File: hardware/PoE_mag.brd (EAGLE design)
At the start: 149.9 x 124.5 mm, 128 parts, among them IC1 LD1117V33, IC10 74LVC1T45SOT23-HAND, IC11 74LVC1T45SOT23-HAND, IC12 PCA9517A, IC2 LD1117V33, IC3 DS1338, IC4 ATMEGA1284, IC5 TSR 1-2450, IC6 LM61, IC7 MCP2200, IC8 74LVC1T45SOT23-HAND, IC9 74LVC1T45SOT23-HAND, Q1 BSS138, Q2 BUK98150-55A, X1 PWR, X2 JTAG, X3 USB, X4 MICRO-SD-SOCKETHIROSE-DM3D, X5 CONN-SMATHD, X6 UFL, X7 22-23-2021, X8 RJ45, X9 RJ11, Y1 32k768, Y2 12MHz, Y3 12MHz

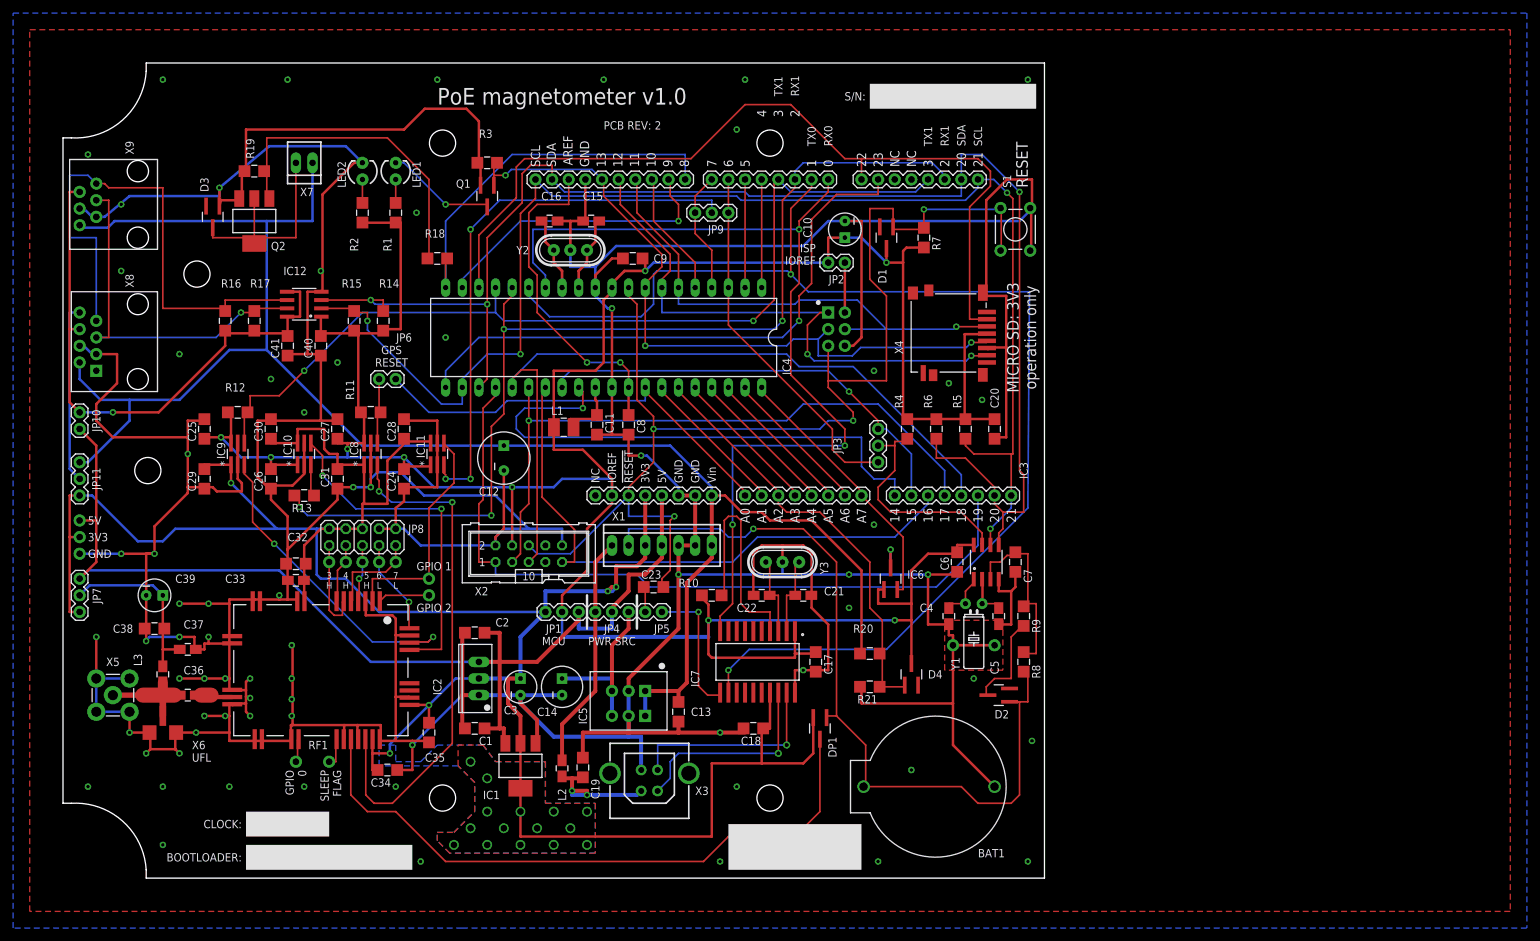
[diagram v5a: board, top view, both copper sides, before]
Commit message: Add cap for RFI suppression across fan, minor track layout changes
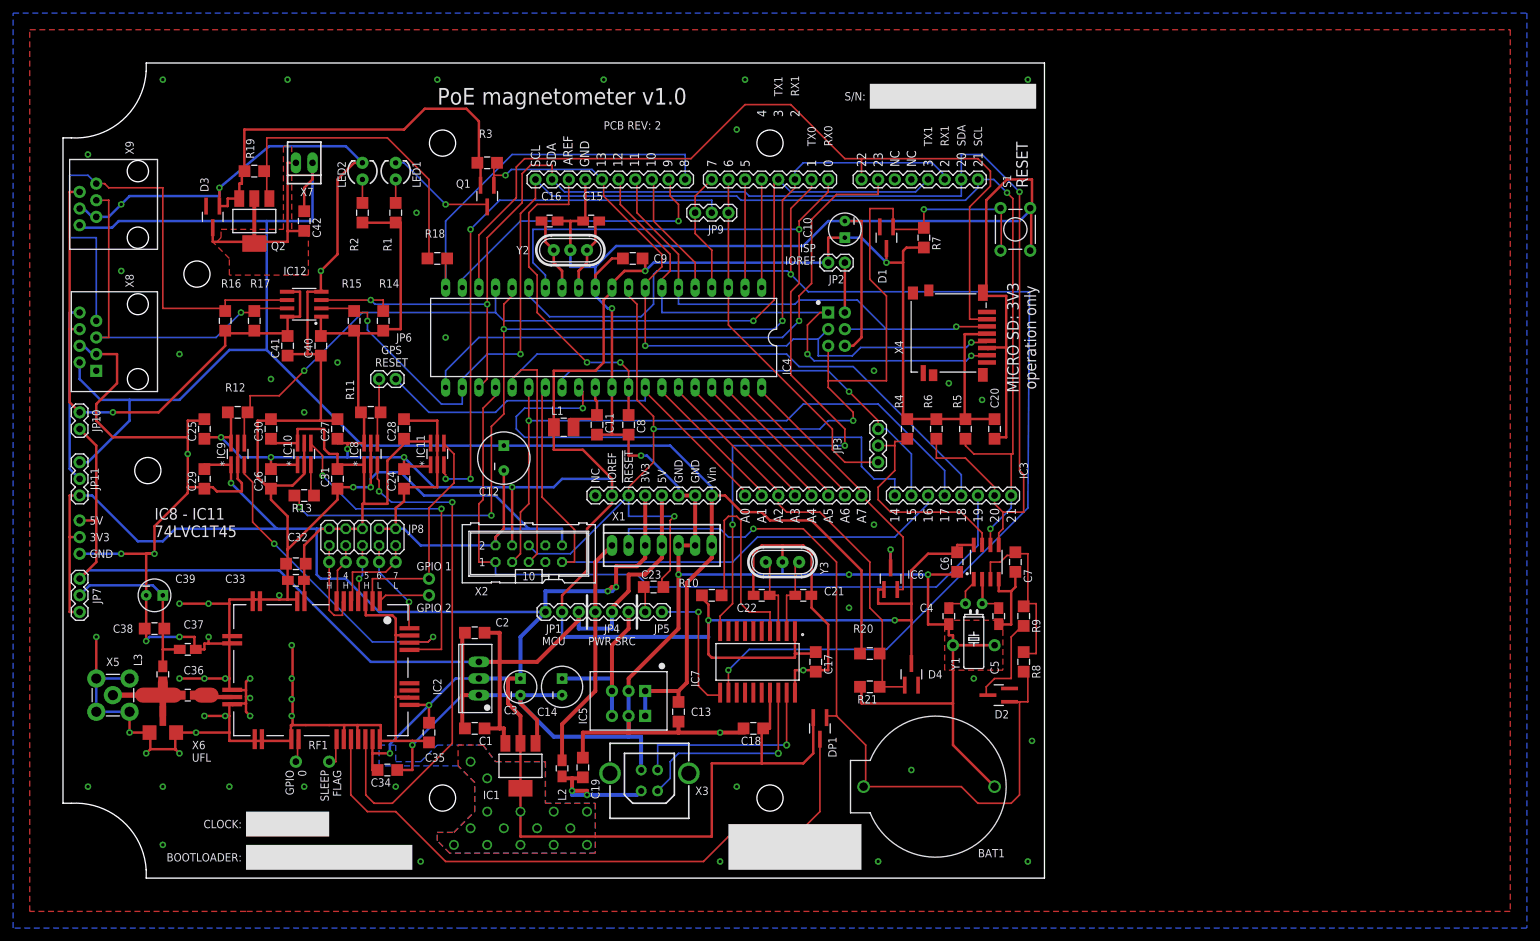
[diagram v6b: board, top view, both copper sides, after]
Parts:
- added C42: 1u, SteveMarple:1206-HAND
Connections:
- net FAN_CTRL: now also C42.2
- net VIN: now also C42.1
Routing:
- net VIN: track 271.2 -> 279.1 mm
- net FAN_CTRL: track 32.6 -> 36.5 mm
- net GND: track 1230.7 -> 1232.4 mm
- added copper zone on layer 1, net FAN_CTRL
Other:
- board text added: "IC8 - IC11 74LVC1T45"
